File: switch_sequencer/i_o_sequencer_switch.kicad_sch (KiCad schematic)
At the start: 11 parts, among them J1 Conn_01x09, J10 3.5mm_Mono_Switched_sm, J11 3.5mm_Mono_Switched_sm, J2 Conn_01x09, J3 3.5mm_Mono_Switched_sm, J4 3.5mm_Mono_Switched_sm, J5 3.5mm_Mono_Switched_sm, J6 3.5mm_Mono_Switched_sm, J7 3.5mm_Mono_Switched_sm, J8 3.5mm_Mono_Switched_sm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

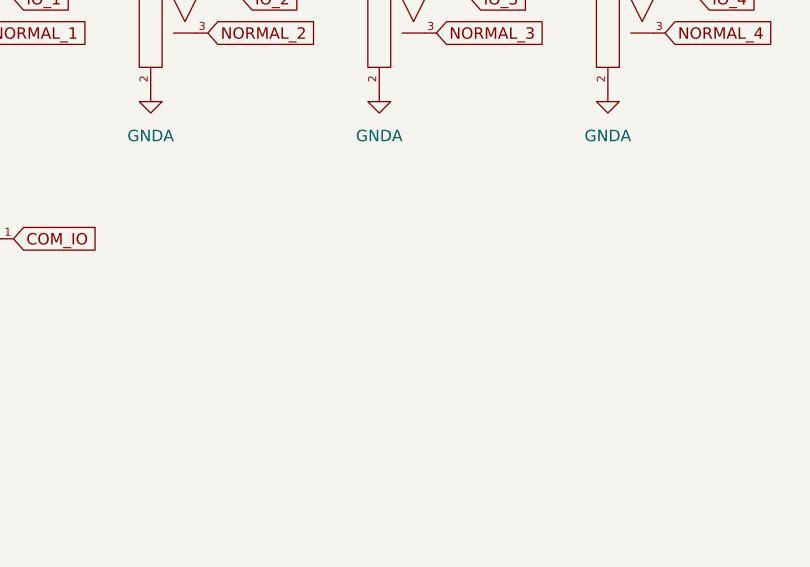
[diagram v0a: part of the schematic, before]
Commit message: Updated schematic of sample and hold, attenuveters, sequential switch
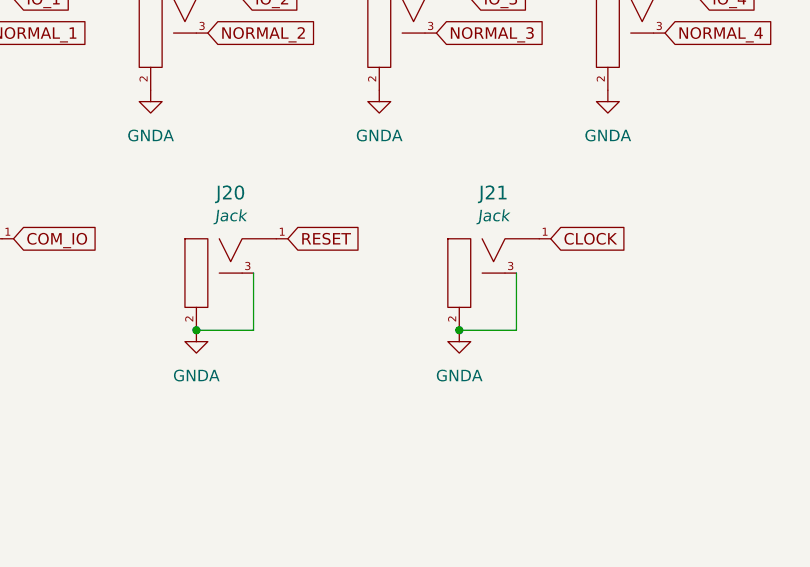
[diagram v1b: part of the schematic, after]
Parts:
- added J20, J21: 3.5mm_Mono_Switched_sm, 4ms_Jack:EighthInch_PJ398SM, symbol 4ms_Jack:3.5mm_Mono_Switched_sm
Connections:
- net GNDA: now also J20.2 (SHEILD), J20.3 (SW), J21.2 (SHEILD), J21.3 (SW)
- new net CLOCK: J21.1 (SIG)
- new net RESET: J20.1 (SIG)
